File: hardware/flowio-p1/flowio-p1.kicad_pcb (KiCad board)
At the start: 4 copper layers, 100 x 80 mm, 164 parts, among them J1 USB-C PWR, J10 VALVE, J11 VALVE, J12 VALVE, J13 VALVE, J14 VALVE, J15 VALVE, J16 VALVE, J17 VALVE, J18 DEBUG-UART, J19 DEBUG-GPIO, J2 USB-C, J20 VALVE, J21 VALVE, J22 VALVE, J23 PUMP, J5 XH-4P, J6 XH-4P, J7 XH-4P, J8 XH-4P, J9 XH-4P, Q10 AO3400A, Q11 SS8050, Q12 SS8050, Q13 AO3400A, Q14 AO3400A, Q15 AO3400A, Q16 AO3400A, Q3 AO3400A, Q4 AO3400A, Q5 AO3400A, Q6 AO3400A, Q7 AO3400A, Q8 AO3400A, Q9 AO3400A, SW1 RST, SW2 BOOT, SW3 USER, U1 ESP32-S3-WROOM-1-N16R8, U2 TCA9548APWR, U3 TPS54331DR, U4 CH340K, U5 USBLC6-2SC6, U6 XGZP6897D, U7 USBLC6-2SC6

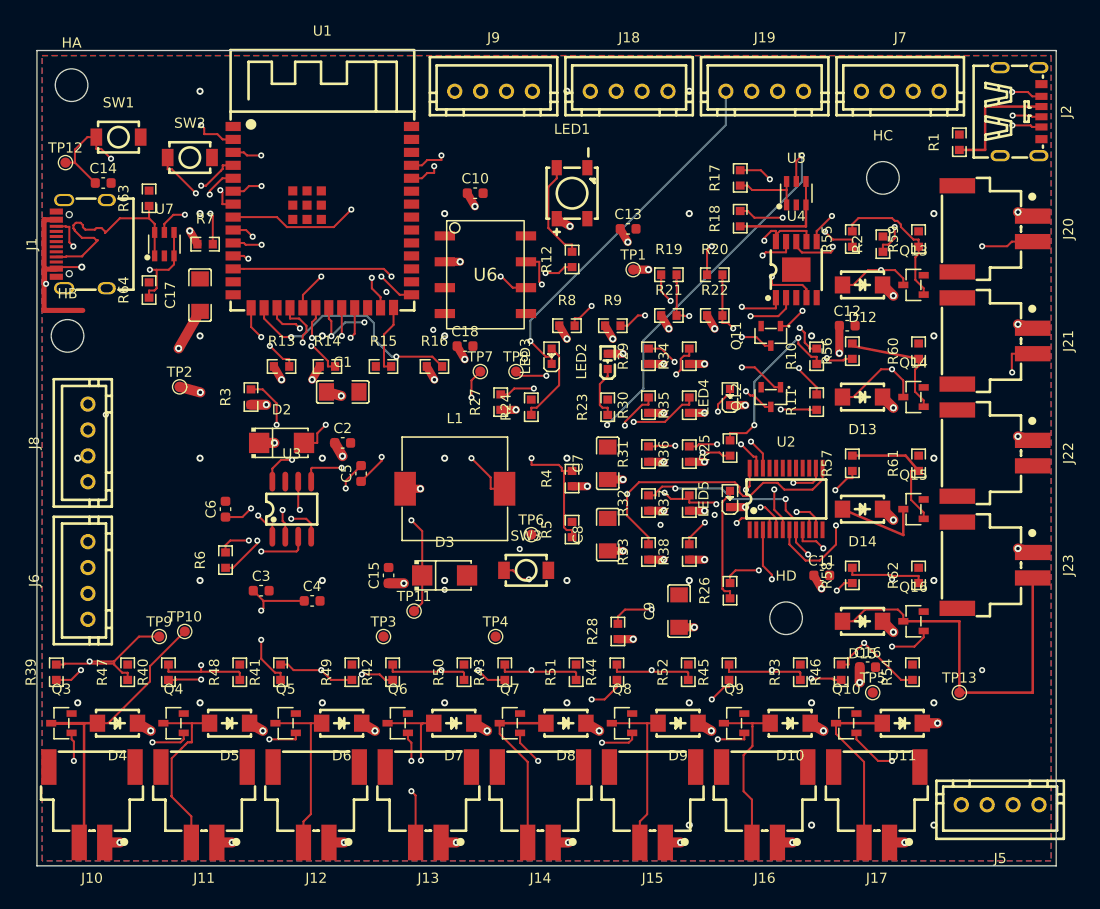
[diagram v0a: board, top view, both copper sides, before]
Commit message: feat(T4d): round5 信号层重布 (In2 纯净化) + 电源重建 — DRC 0 错 (122→60 未连)
- round5: DSN 手术剥 In2 层/In2 平面/电源网 (162 线 125 孔) → freerouting 只在
  F/In1/B 布信号 → SES 导入自动清除全部 In2 信号割线 → 电源平面 refill 复原
- SES 副作用: 电源网铜 (逃逸/缝合/J1 入口) 被连座清除 → stage1/4 全量重建
- seg_clear 层过滤 (F.Cu 引线只避同层走线, 异层下穿无害; 全层检查曾致
  6.5mm 环搜零落点) + spot_free/seg_clear 纳入 freerouting 信号铜为障碍
- 缝合过孔环形搜位 (整格点被信号线压住时 0.9/1.7/2.5mm 偏移)
- VIP 化: 焊盘中心不净空 (内层信号骑 GND 焊盘 / SOP-6 0.65 节距) 自动
  环搜逃逸系锚; J1 过孔落点过 spot_free (P5_CC2 扇出孔同位短路教训)
- 电源逃逸窄线重试/近重复逃逸清理 (一轮多逃逸按焊盘聚类留一)
- Z5NECK 颈桥平面 (6-17,32.5-38) prio6 存活; 左总线 Z5a 锚孔 x2
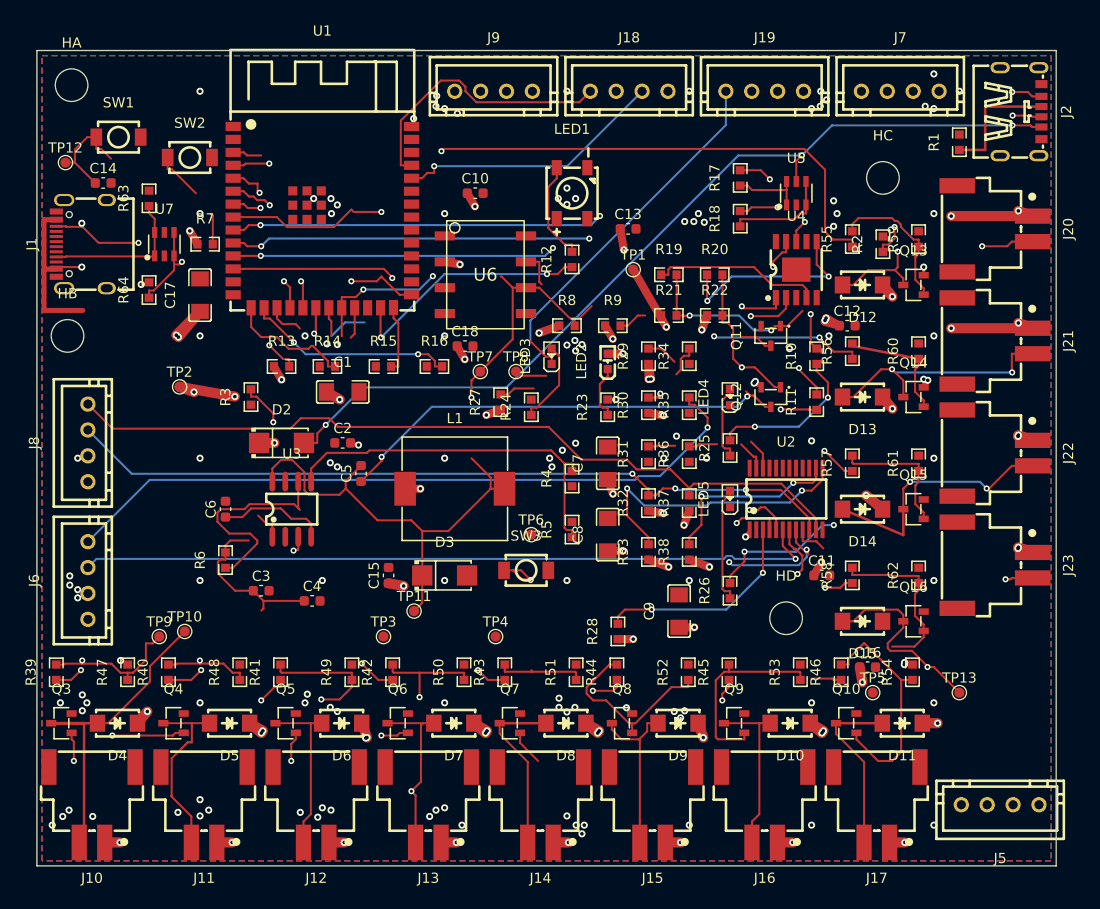
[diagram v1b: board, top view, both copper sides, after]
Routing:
- net +3V3: track 136.1 -> 47.9 mm, vias 41 -> 27
- net EN: track 94.0 -> 19.8 mm, vias 4 -> 0
- net IO21: track 74.2 -> 34.6 mm, vias 3 -> 0
- net I2C_SCL: track 79.7 -> 42.2 mm, vias 5 -> 0
- net I2C_SDA: track 92.0 -> 58.7 mm, vias 5 -> 2
- net S3_SCL: track 76.3 -> 59.1 mm, vias 2 -> 0
- net LED_USER: track 59.8 -> 42.6 mm, vias 3 -> 0
- net S2_SCL: track 109.3 -> 92.7 mm
- net DRV_F: track 9.02 -> 25.2 mm, vias 0 -> 2
- net S2_SDA: track 90.6 -> 103.7 mm, vias 3 -> 2
- net IO10: track 47.1 -> 58.6 mm
- net GND: track 0.00 -> 11.2 mm, vias 35 -> 126
- net GATE8: track 27.4 -> 35.8 mm, vias 2 -> 0
- net COMP: track 13.2 -> 21.2 mm, vias 2 -> 0
- net IO15: track 64.6 -> 72.6 mm
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
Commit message: feat(T4e): stage5/6 收尾 — DRC 0 错 / 17 未连 (338→17)
stage5 (通用修补):
- 电源焊盘窄线重试 (0.6/0.4) + via-in-pad 兜底 (own-pad 跳过/环半径参数化)
- GND F.Cu 孤岛系锚 / 断层补孔 (F↔In1/B 端点重合) / 跨层断头缝合 (孔+jog 净空核验)
- 同层断段 L 补线: 触接图 union-find 真悬空端判定 (防已连通链冗余平行线)
- 阶梯 L 候选 (中点偏移 4 弯绕行)
stage6 (定点收尾, 显式坐标+运行时核验+0.25mm 栅格 A*):
- 同点异层补孔 x5 (S1_SCL/S3_SCL/GATE8/BTN/S1_SDA)
- B.Cu 长线: EN 三段 (SW2↔stub↔U1.3↔东侧 52mm), LED_USER span, I2C_SCL×2, I2C_SDA 斜线, J5/J6/J8 3V3 THT (J5 绕铜柱环)
- 电源滞留 B.Cu 汇流 x8 (锚=HitTestFilledArea 真值, 防 In2 碎片假锚)
- 微缺口跳线 x244 / 跨层端点补孔 / track() 零长段守卫
- U3.2/U7.5/LED4/LED5/R31/R36/C9/U2.24 电源滞留全部接通
铁律执行: 每步 DRC 差分 (0 错保持); del_bad_via 铜柱环清扫 x1
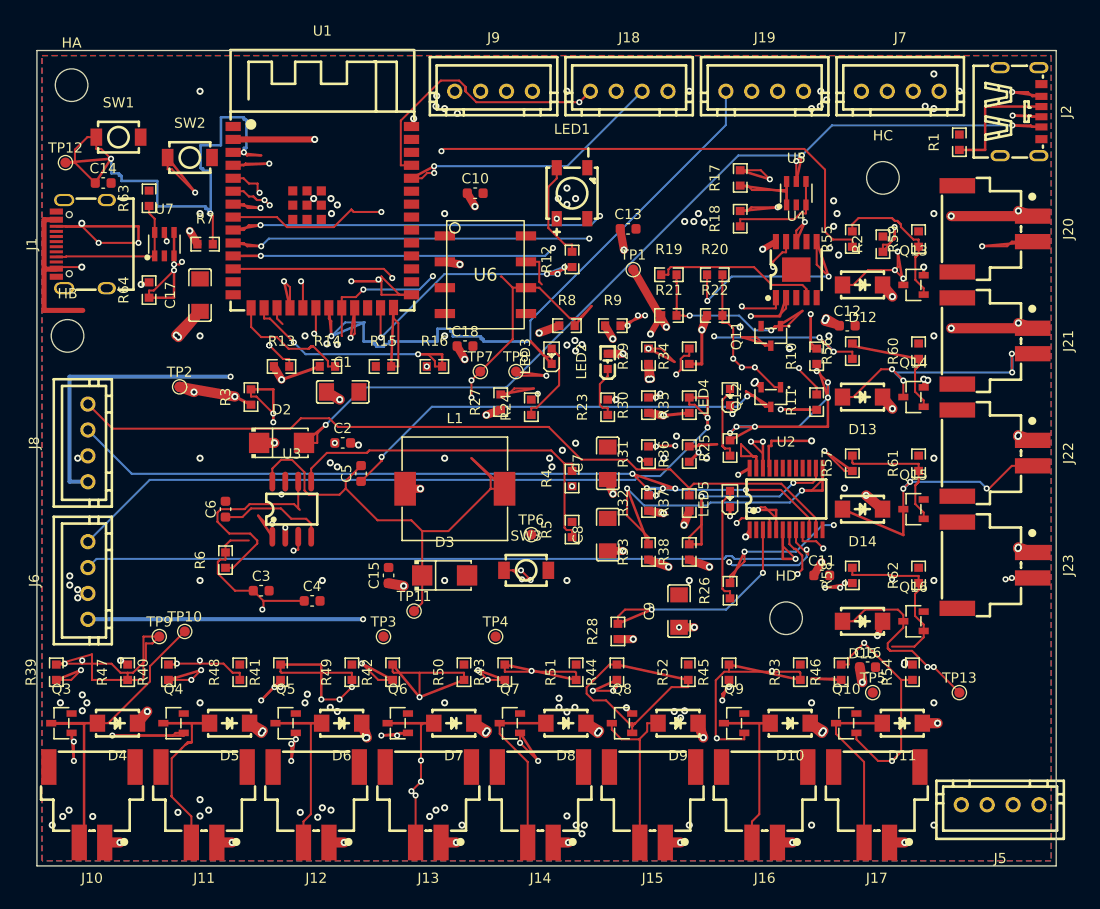
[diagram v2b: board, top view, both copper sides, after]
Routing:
- net +3V3: track 47.9 -> 132.3 mm, vias 27 -> 42
- net EN: track 19.8 -> 71.2 mm, vias 0 -> 3
- net LED_USER: track 42.6 -> 75.6 mm, vias 0 -> 1
- net P5_CC2: track 26.5 -> 58.5 mm, vias 3 -> 6
- net CH_TX: track 36.0 -> 62.9 mm, vias 3 -> 7
- net GATE1: track 27.0 -> 50.4 mm, vias 2 -> 4
- net GATE5: track 21.3 -> 44.1 mm, vias 0 -> 3
- net BOOT: track 137.0 -> 158.2 mm, vias 4 -> 8
- net GATE4: track 18.9 -> 38.2 mm, vias 2 -> 3
- net S1_SDA: track 68.6 -> 85.2 mm, vias 1 -> 2
- net GATE3: track 22.9 -> 39.0 mm, vias 2 -> 6
- net I2C_SCL: track 42.2 -> 56.0 mm, vias 0 -> 6
- net USB_VBUS: track 95.5 -> 107.6 mm, vias 4 -> 5
- net DRV_S: track 23.1 -> 34.8 mm, vias 2 -> 4
- net GATE2: track 27.2 -> 37.8 mm, vias 2 -> 3
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
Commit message: feat(T4g): 残余 17→4 未连手工收官 — DRC 0 错
- BOOT: via282 复用 + In1 竖线 x22.4 平移(避 IO10 平行锁死 0.437mm)
- LED_USER: F 南逃 + B 顶孔北口 (USB_VBUS 对角线口袋北侧)
- I2C_SDA: U 型环 F 顶带 + 微桥 via1+B 环
- I2C_SCL 西东: via(23.555,26)+B y21.3 干线+via268 直达
- S3_SCL/S3_SDA/EN/U4-3V3/J5-3V3: B 层走廊
- IO21: 北环 y8.8 越顶接 Z 形线 + 东干线 x79.5/x80/x83.2 + B南跨
- GND: 孤立孔清理+岛缝合+J7.2/C18.2/J18.2/J5.2 实连
- 剩余: 3 GND zone-zone + 1 IO21 东西轨 (SE 三层堡垒区)
- 四套测试绿: 29/0, 15/0+13/0, flows OK, 21<->21/违例 0
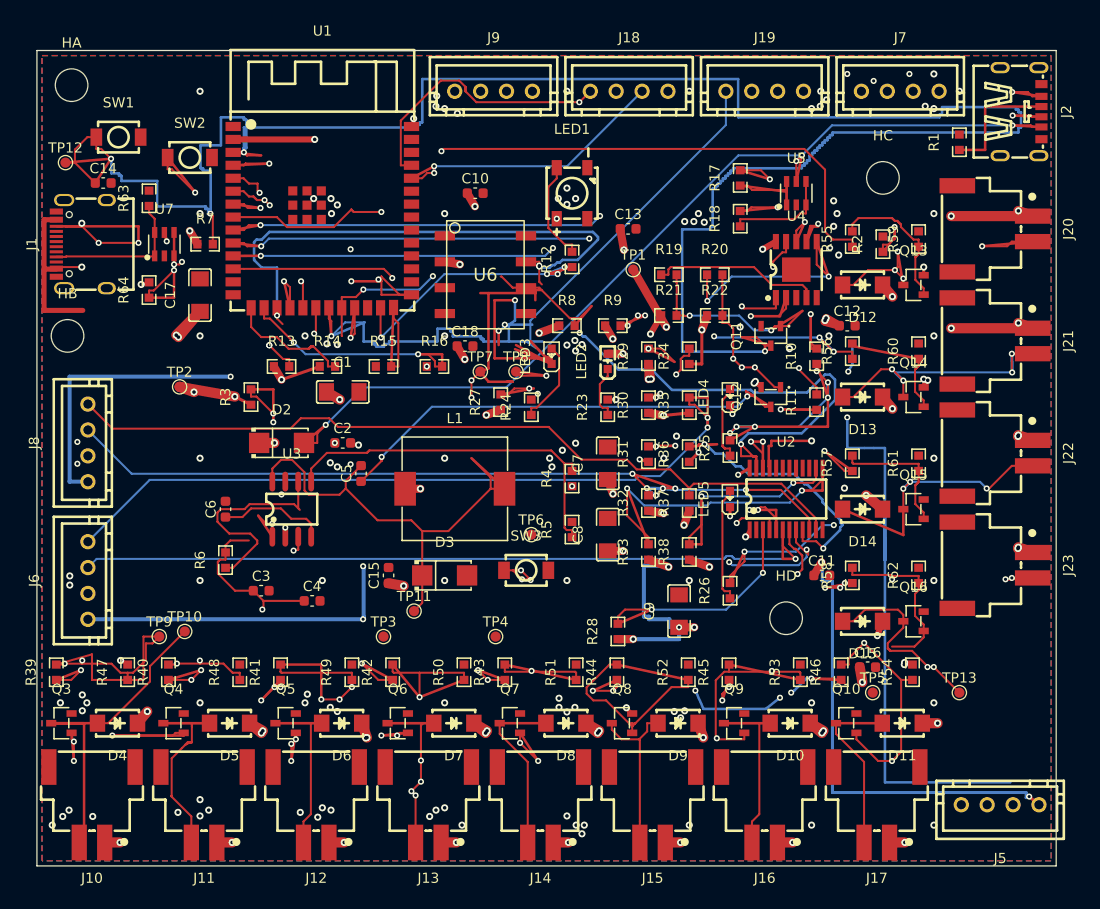
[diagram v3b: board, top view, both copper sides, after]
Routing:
- net IO21: track 40.5 -> 634.1 mm, vias 1 -> 11
- net EN: track 71.2 -> 225.3 mm, vias 3 -> 4
- net +3V3: track 132.3 -> 203.6 mm, vias 42 -> 45
- net I2C_SCL: track 56.0 -> 118.2 mm, vias 6 -> 9
- net I2C_SDA: track 68.0 -> 119.9 mm, vias 3 -> 5
- net LED_USER: track 75.6 -> 109.8 mm, vias 1 -> 4
- net S3_SCL: track 61.8 -> 82.0 mm, vias 1 -> 2
- net BOOT: track 158.2 -> 159.9 mm
- net GND: vias 131 -> 130
- net BTN_USER: vias 5 -> 6

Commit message: fix(T4h-a): GND zone-zone 3条缝合 — 未连4→1, DRC持平142w/0e
- fragment级union-find定位3孤立zone组件 (57主+3小)
- 缝合via 0.3/0.6: (70.707,26.726)/(74.325,15.037)/(74.350,23.651) 各F碎片<->B主平面
- 剩余: IO21 东西轨 1条
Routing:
- net GND: vias 130 -> 133
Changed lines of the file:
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@@
+	)
+	(via
+		(at 74.325499 15.037399)
+		(size 0.6)
+		(drill 0.3)
+		(layers "F.Cu" "B.Cu")
+		(net "GND")
 	)
 	(via
@@
 	)
 	(via
+		(at 70.707148 26.726268)
+		(size 0.6)
+		(drill 0.3)
+		(layers "F.Cu" "B.Cu")
+		(net "GND")
+	)
+	(via
 		(at 52.85 29.472243)
 		(size 0.7)
@@
 		(layers "F.Cu" "B.Cu")
 		(net "GND")
+	)
+	(via
+		(at 74.350499 23.6508)
+		(size 0.6)
+		(drill 0.3)
+		(layers "F.Cu" "B.Cu")
+		(net "GND")
